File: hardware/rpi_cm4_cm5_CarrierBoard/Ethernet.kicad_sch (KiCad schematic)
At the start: 11 parts, among them J5 0826-1X1T-32-F

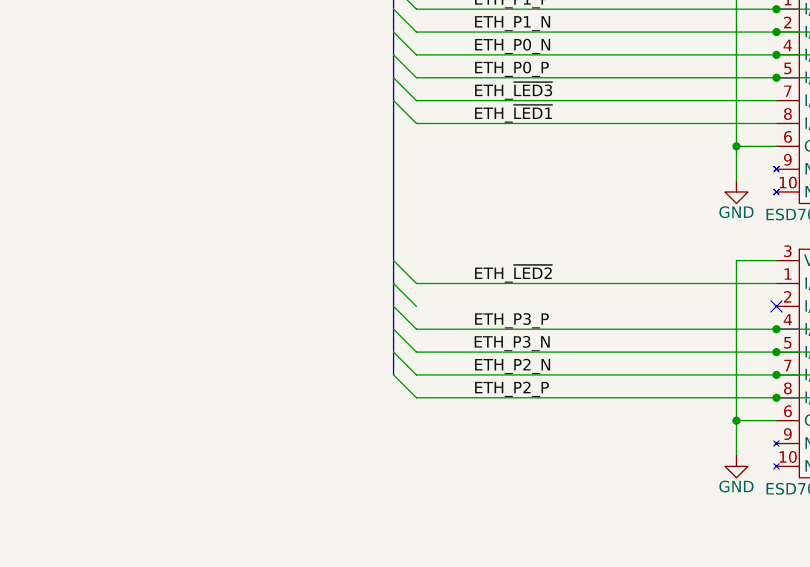
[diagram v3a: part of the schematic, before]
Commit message: Clear ERC markers and cleaned unconnected nets Design freeze
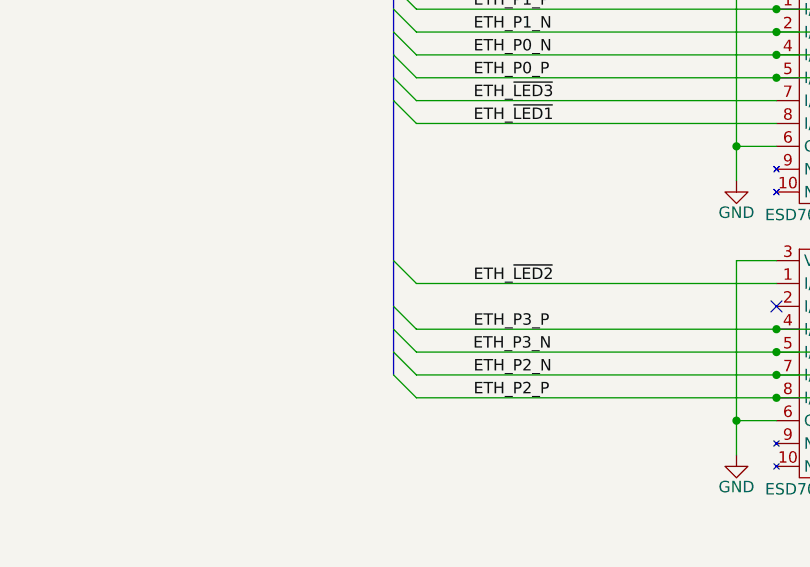
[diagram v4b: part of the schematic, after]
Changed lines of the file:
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@@
 	(title_block
 		(title "RPI CMx Carrier")
-		(date "2026-02-26")
+		(date "2026-02-28")
 		(rev "2.00-0A")
 		(comment 1 "Jean-Francois Bilodeau")
@@
 	)
 	(bus_entry
-		(at 99.06 92.71)
-		(size 2.54 2.54)
-		(stroke
-			(width 0)
-			(type default)
-		)
-	)
-	(bus_entry
 		(at 99.06 97.79)
 		(size 2.54 2.54)
@@
 	(bus
 		(pts
-			(xy 99.06 95.25) (xy 99.06 92.71)
+			(xy 99.06 90.17) (xy 99.06 95.25)
 		)
 		(stroke
@@
 		)
 		(stroke
-			(width 0)
-			(type default)
-		)
-	)
-	(bus
-		(pts
-			(xy 99.06 92.71) (xy 99.06 90.17)
-		)
-		(stroke
